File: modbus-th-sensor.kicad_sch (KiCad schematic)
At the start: 36 parts, among them J1 Screw Terminal, J2 FTDI Serial, J3 ICSP, J4 Sensor Board, J5 Qwiic, SW2 TERM, SW3 Node ID, U1 ATmega328P-A, U3 THVD2410DR, U5 AP63203WU, Y1 8MHz

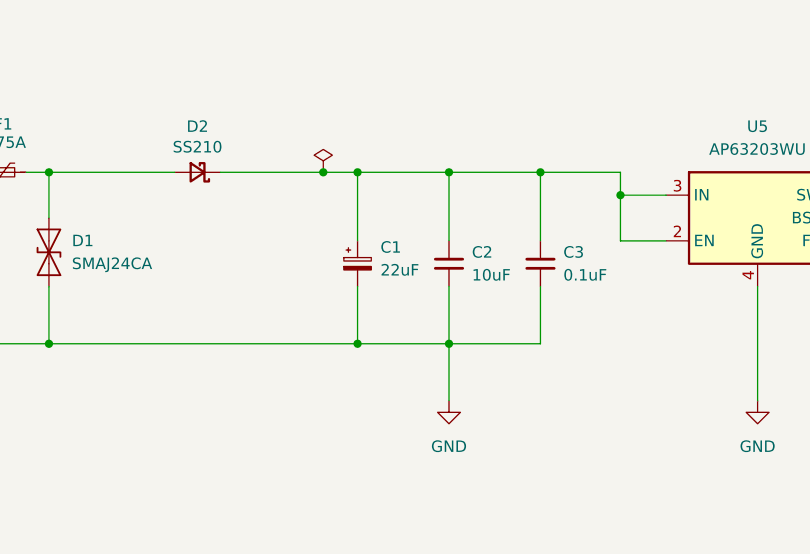
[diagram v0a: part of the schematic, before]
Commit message: Changed C1 to be a 47uF through-hole
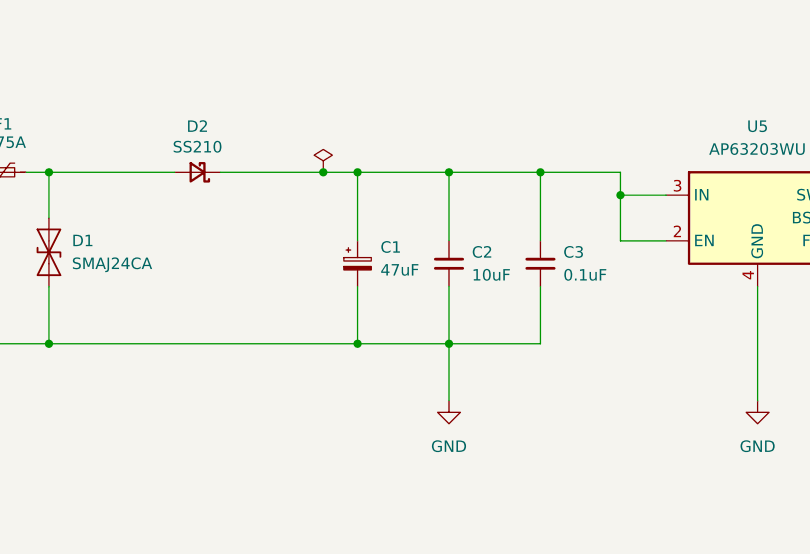
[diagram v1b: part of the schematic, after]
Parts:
- C1: value 22uF -> 47uF; footprint Capacitor_SMD:CP_Elec_6.3x5.8 -> Capacitor_THT:CP_Radial_D6.3mm_P2.50mm; LCSC C336302 -> (none)
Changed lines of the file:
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@@
 			)
 		)
-		(property "Value" "22uF"
+		(property "Value" "47uF"
 			(at 123.19 42.6338 0)
 			(show_name no)
@@
 			)
 		)
-		(property "Footprint" "Capacitor_SMD:CP_Elec_6.3x5.8"
+		(property "Footprint" "Capacitor_THT:CP_Radial_D6.3mm_P2.50mm"
 			(at 120.65 41.91 0)
 			(hide yes)
@@
 			)
 		)
-		(property "LCSC" "C336302"
+		(property "LCSC" ""
 			(at 120.65 41.91 0)
 			(hide yes)

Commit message: Switched some components to Through Hole for hand soldering. Removed components the from pick and place.
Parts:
- removed SW2: TERM, Button_Switch_SMD:SW_DIP_SPSTx01_Slide_6.7x4.1mm_W8.61mm_P2.54mm_LowProfile, symbol Switch:SW_DIP_x01
- removed SW3: Node ID, Button_Switch_SMD:SW_DIP_SPSTx04_Slide_6.7x11.72mm_W8.61mm_P2.54mm_LowProfile, symbol Switch:SW_DIP_x04
- added JP1: Terminate, Connector_PinHeader_2.54mm:PinHeader_1x02_P2.54mm_Vertical, symbol Jumper:Jumper_2_Open
- F1: value 0.75A -> 0.5A; footprint Fuse:Fuse_1812_4532Metric -> Capacitor_THT:C_Disc_D8.0mm_W5.0mm_P5.00mm; LCSC C151170 -> (none)
- J4: now in the parts list
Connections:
- net A: now also JP1.1 (A)
- net at R3.2: now also JP1.2 (B)
- net ID0: no longer names the net of U1.2 (PD4)
- net ID1: no longer names the net of U1.9 (PD5)
- net ID2: no longer names the net of U1.10 (PD6)
- net ID3: no longer names the net of U1.11 (PD7)
- no-connect marks 8 -> 12

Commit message: Changed capacitor C5/C6 part number and footprint
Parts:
- C5, C6: footprint Capacitor_SMD:C_0805_2012Metric -> Capacitor_SMD:C_1206_3216Metric; LCSC C45783 -> C12891
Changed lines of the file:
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@@
 			)
 		)
-		(property "Footprint" "Capacitor_SMD:C_0805_2012Metric"
+		(property "Footprint" "Capacitor_SMD:C_1206_3216Metric"
 			(at 212.09 43.18 0)
 			(hide yes)
@@
 			)
 		)
-		(property "LCSC" "C45783"
+		(property "LCSC" "C12891"
 			(at 212.09 43.18 0)
 			(hide yes)
@@
 			)
 		)
-		(property "Footprint" "Capacitor_SMD:C_0805_2012Metric"
+		(property "Footprint" "Capacitor_SMD:C_1206_3216Metric"
 			(at 200.66 43.18 0)
 			(hide yes)
@@
 			)
 		)
-		(property "LCSC" "C45783"
+		(property "LCSC" "C12891"
 			(at 200.66 43.18 0)
 			(hide yes)

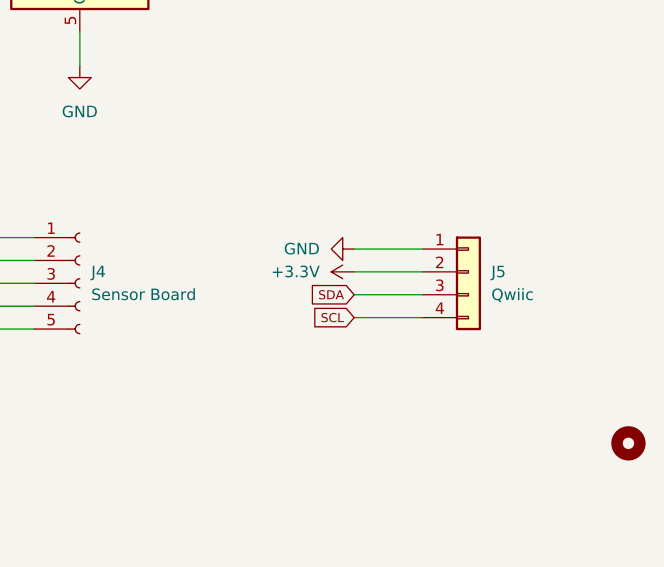
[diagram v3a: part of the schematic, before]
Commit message: Switched to JST PH 2.0mm 4-pin connector footprint for I2C socket I don't plan to populate it - but it is available as a backup. This footprint should be compatible with Adafruit STEMMA and Grove
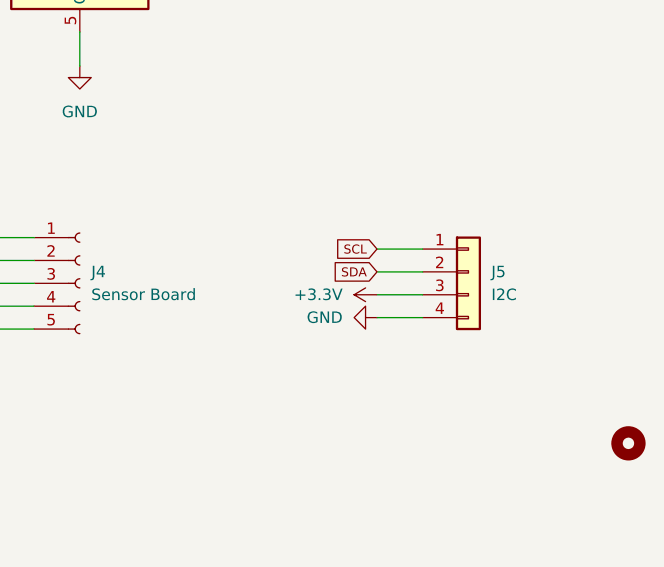
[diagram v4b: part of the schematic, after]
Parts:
- J5: value Qwiic -> I2C; footprint Connector_JST:JST_SH_SM04B-SRSS-TB_1x04-1MP_P1.00mm_Horizontal -> Connector_JST:JST_PH_B4B-PH-K_1x04_P2.00mm_Vertical; LCSC C160404 -> (none); now left out of the parts list
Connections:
- net +3.3V: now also J5.3 (Pin_3); no longer J5.2 (Pin_2)
- net GND: now also J5.4 (Pin_4); no longer J5.1 (Pin_1)
- net SCL: now also J5.1 (Pin_1); no longer J5.4 (Pin_4)
- net SDA: now also J5.2 (Pin_2); no longer J5.3 (Pin_3)
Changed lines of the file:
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@@
 	(wire
 		(pts
-			(xy 162.56 97.79) (xy 162.56 99.06)
+			(xy 251.46 142.24) (xy 256.54 142.24)
 		)
 		(stroke
@@
 	(wire
 		(pts
-			(xy 199.39 97.79) (xy 208.28 97.79)
+			(xy 162.56 97.79) (xy 162.56 99.06)
 		)
 		(stroke
@@
 	(wire
 		(pts
-			(xy 128.27 110.49) (xy 128.27 97.79)
+			(xy 199.39 97.79) (xy 208.28 97.79)
 		)
 		(stroke
@@
 	(wire
 		(pts
-			(xy 248.92 139.7) (xy 256.54 139.7)
+			(xy 128.27 110.49) (xy 128.27 97.79)
 		)
 		(stroke
@@
 	(wire
 		(pts
-			(xy 34.29 147.32) (xy 38.1 147.32)
+			(xy 251.46 144.78) (xy 256.54 144.78)
 		)
 		(stroke
@@
 	(wire
 		(pts
-			(xy 234.95 97.79) (xy 234.95 107.95)
+			(xy 34.29 147.32) (xy 38.1 147.32)
 		)
 		(stroke
@@
 	(wire
 		(pts
-			(xy 121.92 133.35) (xy 118.11 133.35)
+			(xy 234.95 97.79) (xy 234.95 107.95)
 		)
 		(stroke
@@
 	(wire
 		(pts
-			(xy 86.36 31.75) (xy 86.36 36.83)
+			(xy 121.92 133.35) (xy 118.11 133.35)
 		)
 		(stroke
@@
 	(wire
 		(pts
-			(xy 208.28 146.05) (xy 213.36 146.05)
+			(xy 86.36 31.75) (xy 86.36 36.83)
 		)
 		(stroke
@@
 	(wire
 		(pts
-			(xy 118.11 140.97) (xy 121.92 140.97)
+			(xy 208.28 146.05) (xy 213.36 146.05)
 		)
 		(stroke
@@
 	(wire
 		(pts
-			(xy 118.11 151.13) (xy 121.92 151.13)
+			(xy 118.11 140.97) (xy 121.92 140.97)
 		)
 		(stroke
@@
 	(wire
 		(pts
-			(xy 130.81 31.75) (xy 130.81 39.37)
+			(xy 118.11 151.13) (xy 121.92 151.13)
 		)
 		(stroke
@@
 	(wire
 		(pts
-			(xy 248.92 142.24) (xy 256.54 142.24)
+			(xy 130.81 31.75) (xy 130.81 39.37)
 		)
 		(stroke
@@
 	(wire
 		(pts
+			(xy 251.46 139.7) (xy 256.54 139.7)
+		)
+		(stroke
+			(width 0)
+			(type default)
+		)
+	)
+	(wire
+		(pts
 			(xy 176.53 31.75) (xy 176.53 34.29)
 		)
@@
 	(wire
 		(pts
-			(xy 248.92 147.32) (xy 256.54 147.32)
-		)
-		(stroke
-			(width 0)
-			(type default)
-		)
-	)
-	(wire
-		(pts
 			(xy 38.1 113.03) (xy 49.53 113.03)
 		)
@@
 	(wire
 		(pts
-			(xy 248.92 144.78) (xy 256.54 144.78)
-		)
-		(stroke
-			(width 0)
-			(type default)
-		)
-	)
-	(wire
-		(pts
 			(xy 200.66 31.75) (xy 200.66 40.64)
 		)
@@
 	(wire
 		(pts
+			(xy 251.46 147.32) (xy 256.54 147.32)
+		)
+		(stroke
+			(width 0)
+			(type default)
+		)
+	)
+	(wire
+		(pts
 			(xy 130.81 50.8) (xy 140.97 50.8)
 		)
@@
 	(global_label "SCL"
 		(shape input)
-		(at 248.92 147.32 180)
+		(at 251.46 139.7 180)
 		(fields_autoplaced yes)
 		(effects
@@
 		)
 		(property "Intersheetrefs" "${INTERSHEET_REFS}"
-			(at 243.7602 147.32 0)
+			(at 246.3002 139.7 0)
 			(hide yes)
 			(show_name no)
@@
 	(global_label "SDA"
 		(shape input)
-		(at 248.92 144.78 180)
+		(at 251.46 142.24 180)
 		(fields_autoplaced yes)
 		(effects
@@
 		)
 		(property "Intersheetrefs" "${INTERSHEET_REFS}"
-			(at 243.7602 144.78 0)
+			(at 246.3002 142.24 0)
 			(hide yes)
 			(show_name no)
@@
 	(symbol
 		(lib_id "power:+3.3V")
-		(at 248.92 142.24 90)
+		(at 251.46 144.78 90)
 		(unit 1)
 		(body_style 1)
@@
 		(dnp no)
 		(property "Reference" "#PWR028"
-			(at 252.73 142.24 90)
+			(at 255.27 144.78 90)
 			(hide yes)
 			(show_name no)
@@
 		)
 		(property "Value" "+3.3V"
-			(at 245.11 142.24 90)
+			(at 247.65 144.78 90)
 			(show_name no)
 			(do_not_autoplace no)
@@
 		)
 		(property "Footprint" ""
-			(at 248.92 142.24 0)
+			(at 251.46 144.78 0)
 			(hide yes)
 			(show_name no)
@@
 		)
 		(property "Datasheet" ""
-			(at 248.92 142.24 0)
+			(at 251.46 144.78 0)
 			(hide yes)
 			(show_name no)
@@
 		)
 		(property "Description" "Power symbol creates a global label with name \"+3.3V\""
-			(at 248.92 142.24 0)
+			(at 251.46 144.78 0)
 			(hide yes)
 			(show_name no)
@@
 		(body_style 1)
 		(exclude_from_sim no)
-		(in_bom yes)
+		(in_bom no)
 		(on_board yes)
-		(in_pos_files yes)
+		(in_pos_files no)
 		(dnp no)
 		(property "Reference" "J5"
@@
 			)
 		)
-		(property "Value" "Qwiic"
+		(property "Value" "I2C"
 			(at 264.16 144.78 0)
 			(show_name no)
@@
 			)
 		)
-		(property "Footprint" "Connector_JST:JST_SH_SM04B-SRSS-TB_1x04-1MP_P1.00mm_Horizontal"
-			(at 261.62 142.24 0)
-			(hide yes)
-			(show_name no)
-			(do_not_autoplace no)
-			(effects
-				(font
-					(size 1.27 1.27)
-				)
-			)
-		)
-		(property "Datasheet" "https://www.jst-mfg.com/product/pdf/eng/eSH.pdf"
+		(property "Footprint" "Connector_JST:JST_PH_B4B-PH-K_1x04_P2.00mm_Vertical"
 			(at 261.62 142.24 0)
 			(hide yes)
@@
 			)
 		)
-		(property "Description" "JST SH 1.0mm 4-pin connector (SparkFun Qwiic)"
+		(property "Datasheet" "https://www.jst-mfg.com/product/index.php?series=199"
 			(at 261.62 142.24 0)
 			(hide yes)
@@
 			)
 		)
-		(property "LCSC" "C160404"
+		(property "Description" "JST PH 2.0mm 4-pin connector (Adafruit STEMMA)"
 			(at 261.62 142.24 0)
 			(hide yes)
@@
 	(symbol
 		(lib_id "power:GND")
-		(at 248.92 139.7 270)
+		(at 251.46 147.32 270)
 		(unit 1)
 		(body_style 1)
@@
 		(dnp no)
 		(property "Reference" "#PWR027"
-			(at 242.57 139.7 270)
+			(at 245.11 147.32 270)
 			(hide yes)
 			(show_name no)
@@
 		)
 		(property "Value" "GND"
-			(at 245.11 139.7 90)
+			(at 247.65 147.32 90)
 			(show_name no)
 			(do_not_autoplace no)
@@
 		)
 		(property "Footprint" ""
-			(at 248.92 139.7 0)
+			(at 251.46 147.32 0)
 			(hide yes)
 			(show_name no)
@@
 		)
 		(property "Datasheet" ""
-			(at 248.92 139.7 0)
+			(at 251.46 147.32 0)
 			(hide yes)
 			(show_name no)
@@
 		)
 		(property "Description" "Power symbol creates a global label with name \"GND\" , ground"
-			(at 248.92 139.7 0)
+			(at 251.46 147.32 0)
 			(hide yes)
 			(show_name no)

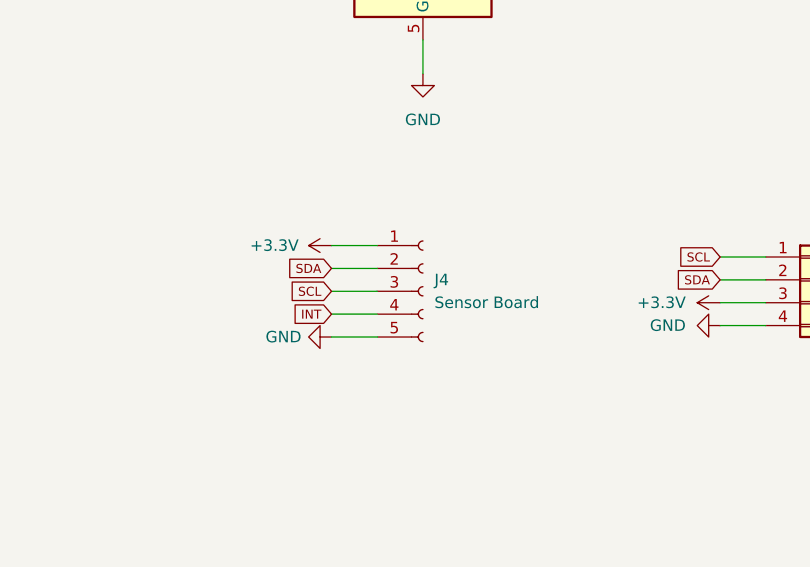
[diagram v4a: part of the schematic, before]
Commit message: Added (mirror x) to the sensor board header
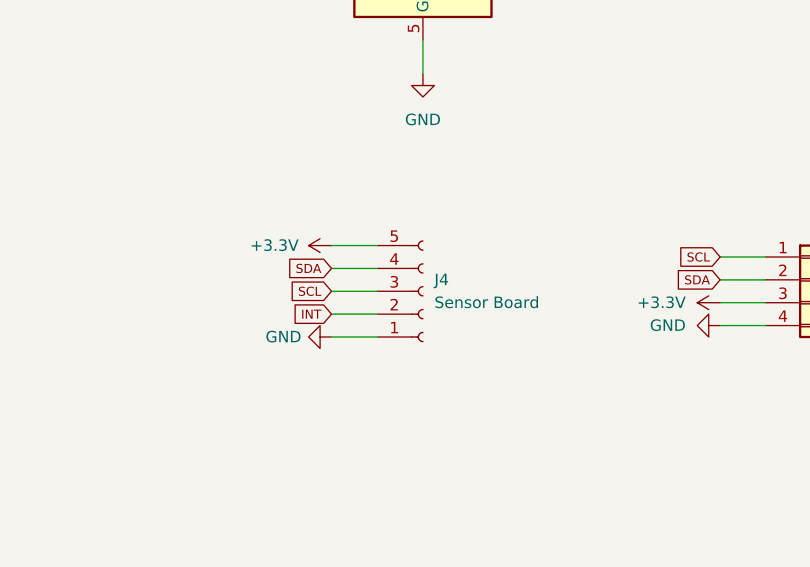
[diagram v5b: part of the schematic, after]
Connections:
- net +3.3V: now also J4.5 (Pin_5); no longer J4.1 (Pin_1)
- net GND: now also J4.1 (Pin_1); no longer J4.5 (Pin_5)
- net INT: now also J4.2 (Pin_2); no longer J4.4 (Pin_4)
- net SDA: now also J4.4 (Pin_4); no longer J4.2 (Pin_2)
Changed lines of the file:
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@@
 		(lib_id "Connector:Conn_01x05_Socket")
 		(at 218.44 143.51 0)
+		(mirror x)
 		(unit 1)
 		(body_style 1)

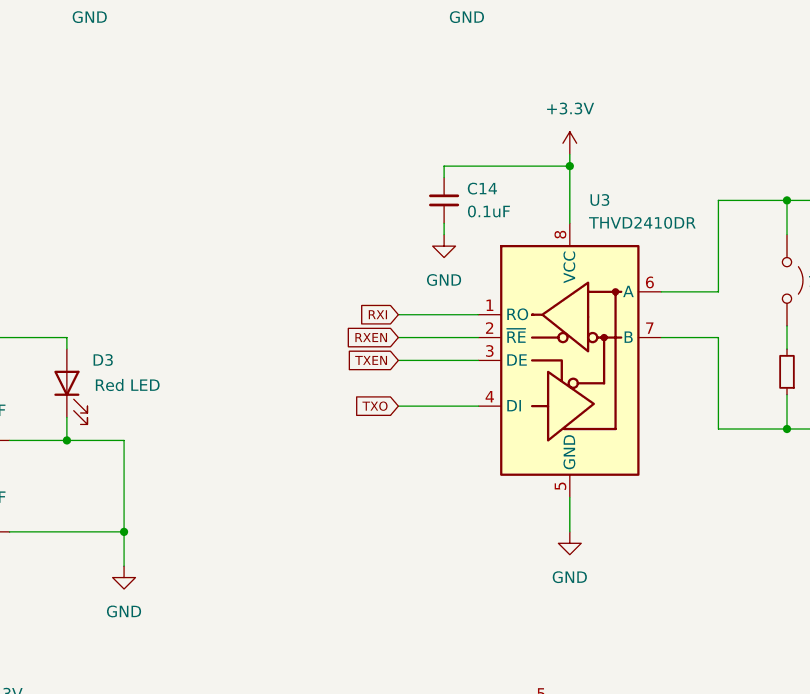
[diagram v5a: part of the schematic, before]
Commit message: Added pull-up resistors to RS-485 interface
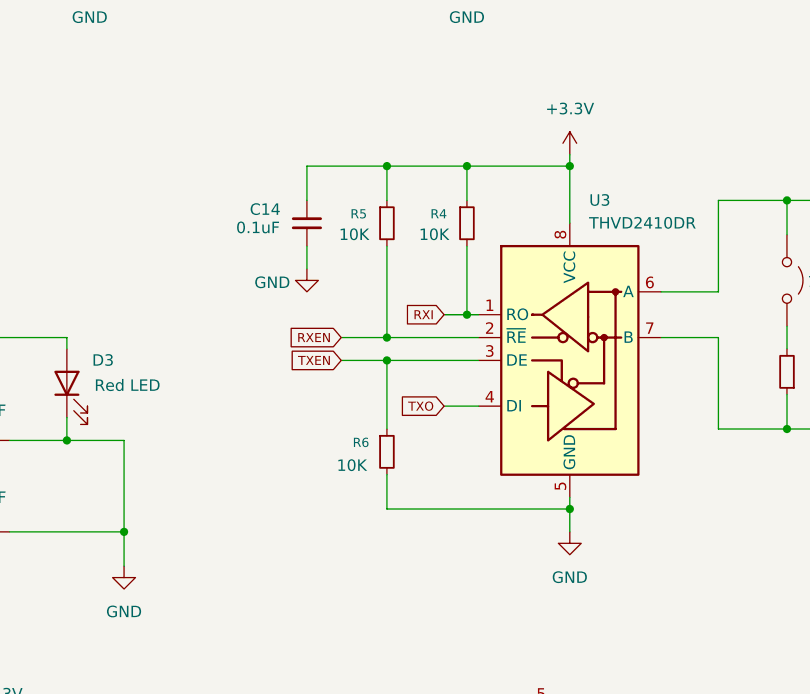
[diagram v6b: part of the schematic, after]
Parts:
- added R4, R5, R6: 10K, Resistor_SMD:R_0603_1608Metric, symbol Device:R_Small
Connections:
- net +3.3V: now also R4.1, R5.1
- net GND: now also R6.2
- net RXEN: now also R5.2
- net RXI: now also R4.2
- net TXEN: now also R6.1
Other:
- moved on the sheet: C14

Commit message: Added Kefa HT396 footprints
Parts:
- J1: footprint Connector_Phoenix_MC:PhoenixContact_MCV_1,5_4-G-3.5_1x04_P3.50mm_Vertical -> Kefa HT396:Kefa_HT396R-3.96-04P_1x04_P3.96mm_Horizontal
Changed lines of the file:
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@@
 			)
 		)
-		(property "Footprint" "Connector_Phoenix_MC:PhoenixContact_MCV_1,5_4-G-3.5_1x04_P3.50mm_Vertical"
+		(property "Footprint" "Kefa HT396:Kefa_HT396R-3.96-04P_1x04_P3.96mm_Horizontal"
 			(at 36.83 72.39 0)
 			(hide yes)
